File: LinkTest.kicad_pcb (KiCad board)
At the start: 4 copper layers, 62 x 70 mm, 79 parts, among them J2 Conn_01x04_Socket, J4 Conn_01x01, J5 Conn_01x01, Q1 IRLML2803, Q2 IRLML2803, U1 RFM98PW, U2 TPS54426PWPR, U3 LORA1280F27-TCXO, U4 ADM1176-1ARMZ-R7

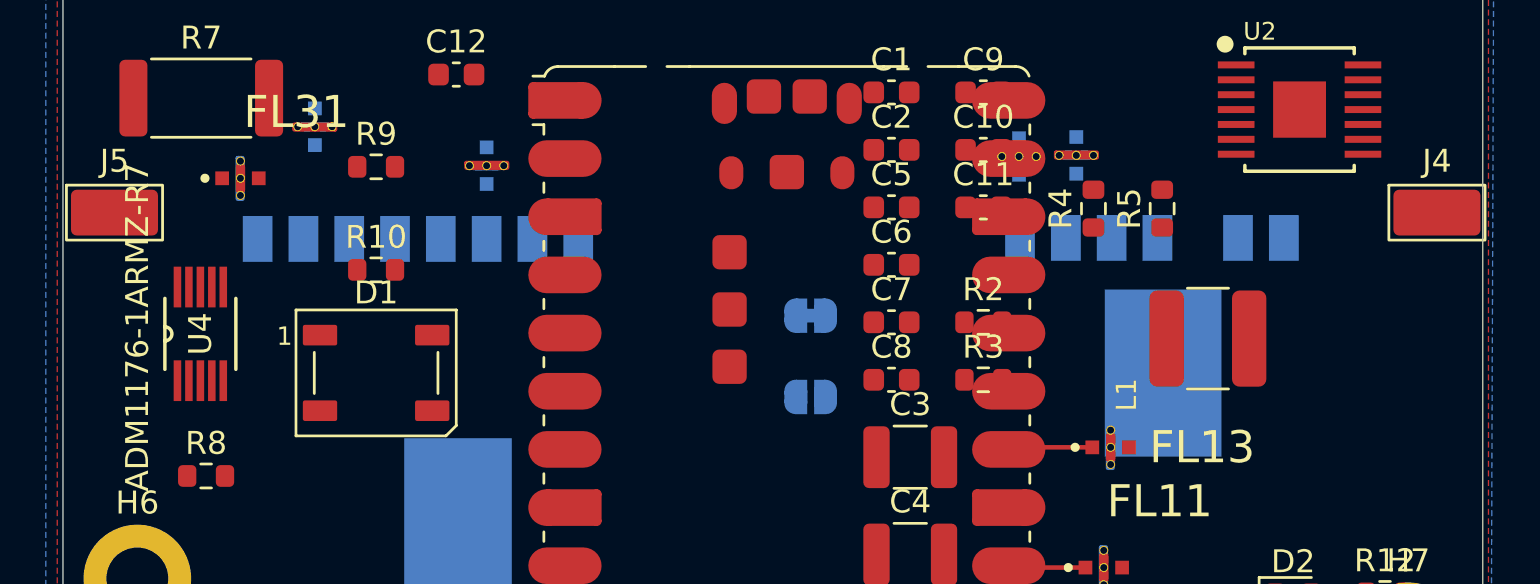
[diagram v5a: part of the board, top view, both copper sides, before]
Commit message: 50 ohm netclass
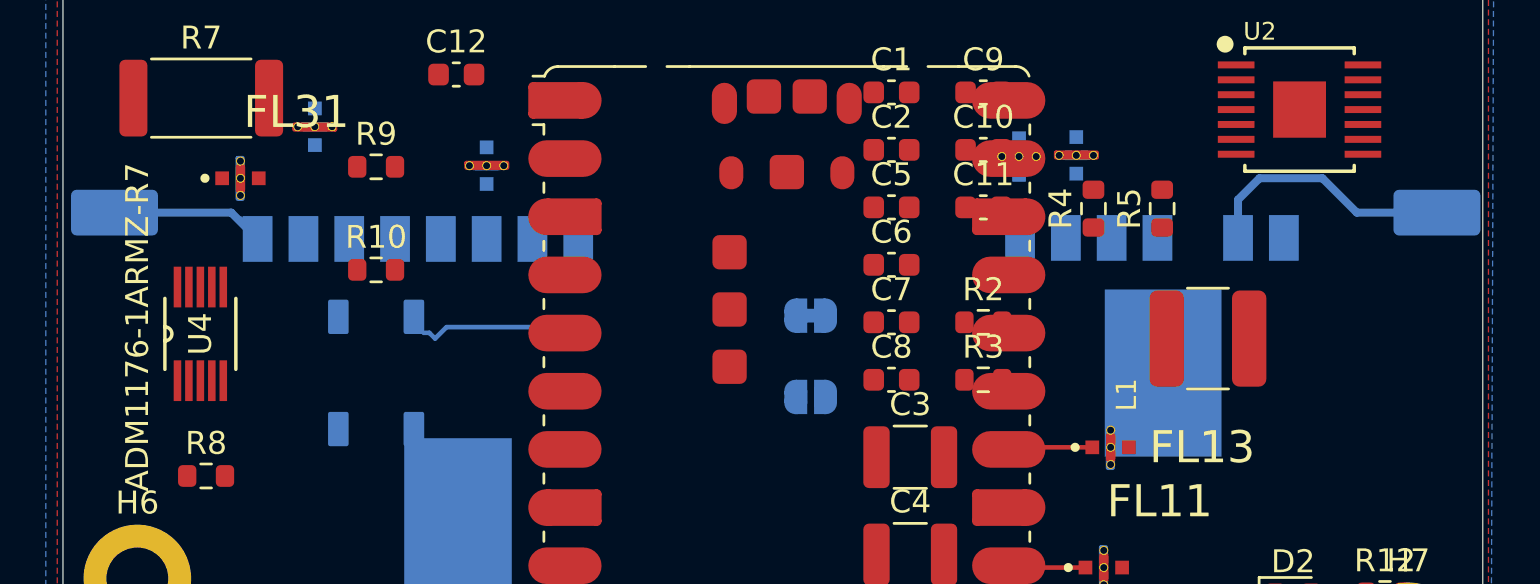
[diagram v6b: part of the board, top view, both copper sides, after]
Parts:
- D1, J4, J5: moved to B.Cu
- turned D1 to 90 degrees
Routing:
- net Net-(J4-Pin_1): track 0.00 -> 11.4 mm
- net /UHF_ANT: track 0.00 -> 8.19 mm
- net /NEOPIXEL: track 0.00 -> 6.06 mm

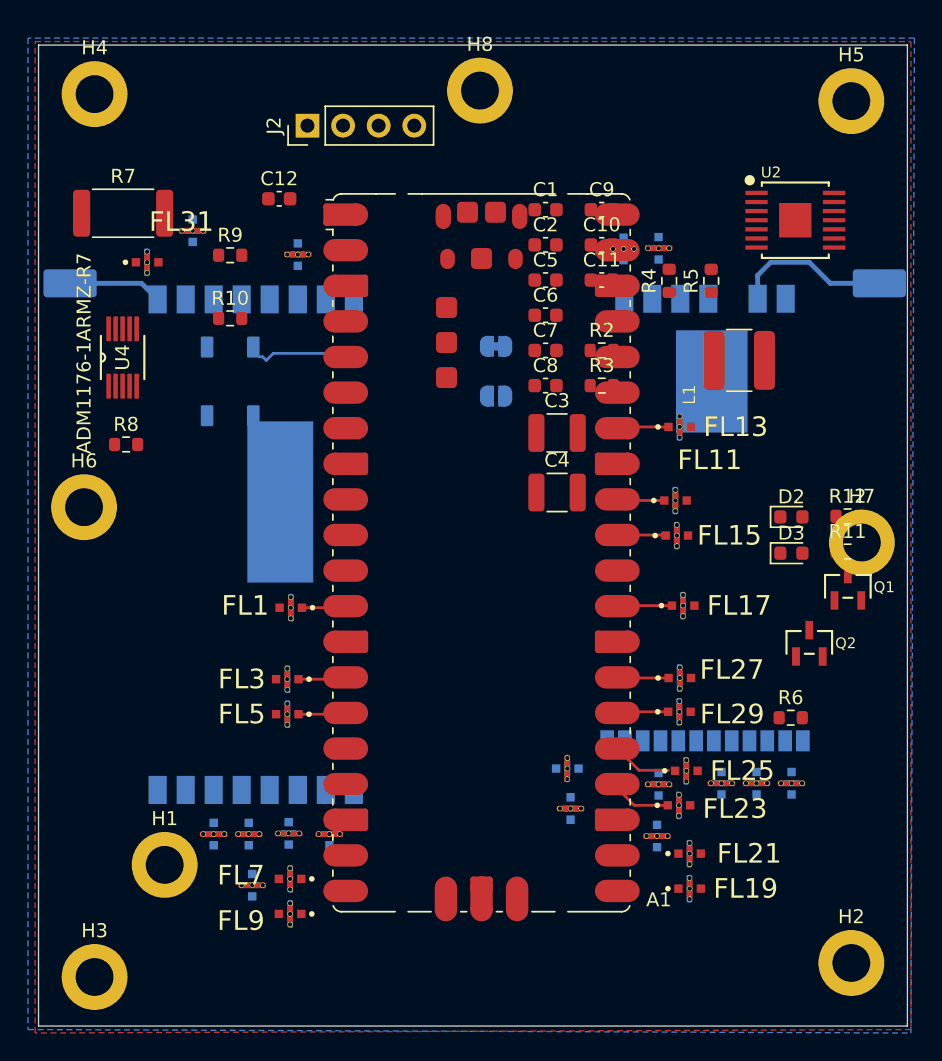
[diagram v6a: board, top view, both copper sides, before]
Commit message: Power Monitor and 5V reg laid out; mechanicals on USER1 layer
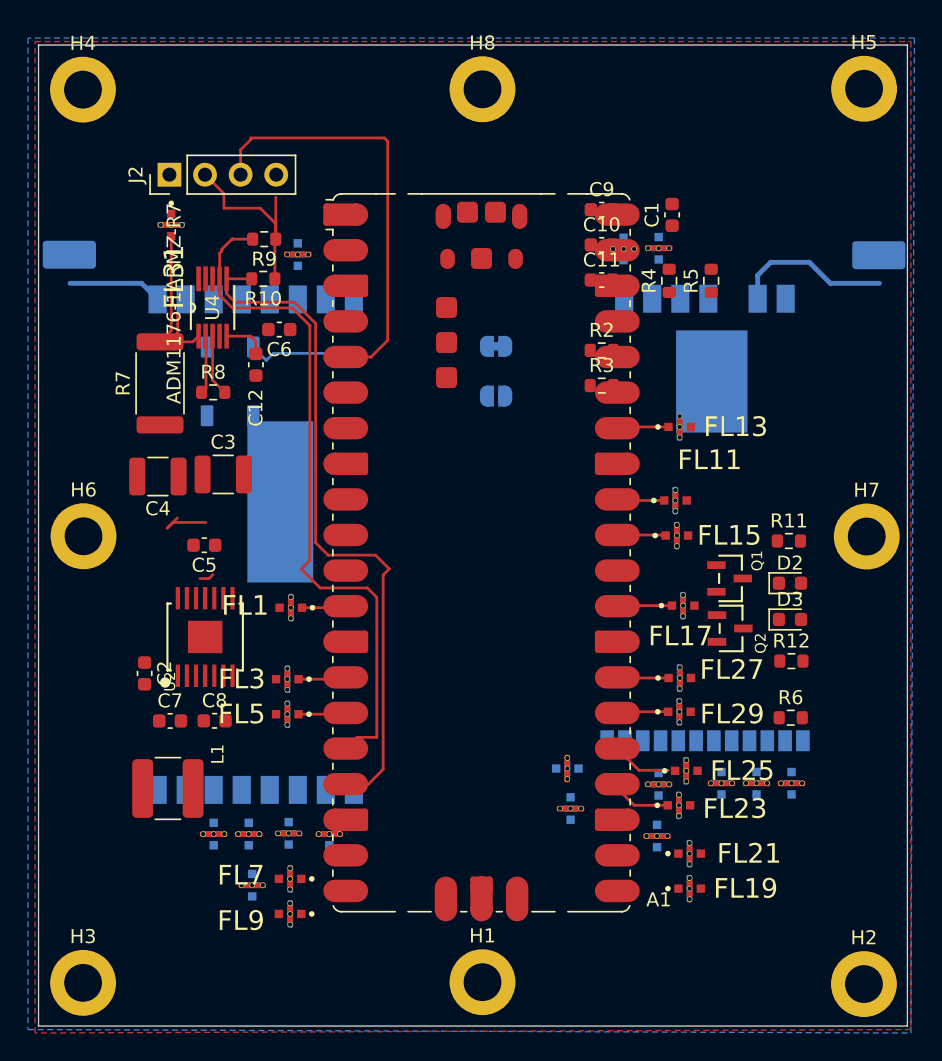
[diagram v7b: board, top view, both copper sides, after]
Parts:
- removed FL32: NFM18CC101R1C3D, NFM18CC101R1C3D:FIL_NFM18CC101R1C3D
- moved U2 51.6 mm to (133.9, 105.7), turned to 90 degrees
- moved L1 50.9 mm to (131.2, 116.5), turned to 180 degrees
- moved C2 41.9 mm to (129.6, 108.3), turned to -90 degrees
- moved C7 37.6 mm to (131.4, 111.7)
- moved C8 33.6 mm to (134.6, 111.7)
- moved C5 30.8 mm to (133.8, 99.2), turned to 180 degrees
- moved C4 28.5 mm to (130.5, 94.3), turned to 180 degrees
- moved H1 24.2 mm to (153.7, 130.4)
- moved C3 24.0 mm to (135.2, 94.1)
- moved C6 19.0 mm to (139.2, 83.8), turned to 180 degrees
- moved R7 12.4 mm to (130.7, 87.6), turned to 90 degrees
- moved C12 12.0 mm to (137.5, 86.3), turned to 90 degrees
- moved R12 11.1 mm to (175.7, 107.5)
- moved J2 10.5 mm to (131.3, 72.8)
- moved C1 9.04 mm to (167.2, 75.6), turned to 90 degrees
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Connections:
- FL31 pad 3: Net-(FL31-Pad3) -> VBATT_SENSE
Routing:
- net SDA_PWR: track 0.00 -> 49.6 mm
- net SCL_PWR: track 0.00 -> 49.4 mm
- net /NEOPIXEL: track 6.06 -> 36.5 mm
- net 3.3V: track 0.00 -> 14.1 mm
- net VBATT_SENSE: track 0.00 -> 13.4 mm
- net Net-(U4-ON): track 0.00 -> 4.37 mm
- net VBATT: track 0.00 -> 4.15 mm
- net GND: track 0.00 -> 3.93 mm
- net Net-(U4-TIMER): track 0.00 -> 3.15 mm
- net Net-(U2-SW1): track 0.00 -> 1.04 mm
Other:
- board text added: "Sidewall thickness (mm) MCU/TOP 11.5 Radio 5.0 SMA 15.0 inside Screw Holes (mm) Diameter 3 From Edge 3 Width 57 Height 65"
